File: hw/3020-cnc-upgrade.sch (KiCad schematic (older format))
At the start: 10 parts, among them P1 CONN_01X02, P2 CONN_01X03, P3 CONN_01X08, P4 CONN_01X03, U1 6N136, U2 arduino_pro_micro, U3 MCP41010

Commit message: updated
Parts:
- U2: footprint (none) -> Housings_DIP:DIP-24_W15.24mm
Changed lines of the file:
@@
 F 0 "U2" H 5075 4625 60  0000 C CNN
 F 1 "arduino_pro_micro" H 5275 3225 60  0000 C CNN
-F 2 "" H 5275 3875 60  0001 C CNN
+F 2 "Housings_DIP:DIP-24_W15.24mm" H 5275 3875 60  0001 C CNN
 F 3 "" H 5275 3875 60  0001 C CNN
 	1    5275 3925
@@
 	7500 4375 8100 4375
 $Comp
-L GND #PWR4
+L GND #PWR01
 U 1 1 5A728854
 P 7100 4850
-F 0 "#PWR4" H 7100 4600 50  0001 C CNN
+F 0 "#PWR01" H 7100 4600 50  0001 C CNN
 F 1 "GND" H 7100 4700 50  0000 C CNN
 F 2 "" H 7100 4850 50  0000 C CNN
@@
 	7100 4850 7100 4675
 $Comp
-L +5V #PWR3
+L +5V #PWR02
 U 1 1 5A728882
 P 7100 3675
-F 0 "#PWR3" H 7100 3525 50  0001 C CNN
+F 0 "#PWR02" H 7100 3525 50  0001 C CNN
 F 1 "+5V" H 7100 3815 50  0000 C CNN
 F 2 "" H 7100 3675 50  0000 C CNN
@@
 $EndComp
 $Comp
-L GND #PWR1
+L GND #PWR03
 U 1 1 5A728A6B
 P 3200 4025
-F 0 "#PWR1" H 3200 3775 50  0001 C CNN
+F 0 "#PWR03" H 3200 3775 50  0001 C CNN
 F 1 "GND" H 3200 3875 50  0000 C CNN
 F 2 "" H 3200 4025 50  0000 C CNN
@@
 $EndComp
 $Comp
-L +5V #PWR2
+L +5V #PWR04
 U 1 1 5A72942B
 P 3350 3175
-F 0 "#PWR2" H 3350 3025 50  0001 C CNN
+F 0 "#PWR04" H 3350 3025 50  0001 C CNN
 F 1 "+5V" H 3350 3315 50  0000 C CNN
 F 2 "" H 3350 3175 50  0000 C CNN

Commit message: pcb layout
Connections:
- net ~CS: now reaches U2.13 (10), U3.1 (~CS)
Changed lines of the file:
@@
 Text Label 6050 4075 2    60   ~ 0
 POT
+Text Label 5825 4475 0    60   ~ 0
+~CS
 $EndSCHEMATC

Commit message: minor updates to hw
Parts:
- U1: symbol 6N136 -> 6N136-RESCUE-3020-cnc-upgrade
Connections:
- net +5V: now also P4.3 (P3); no longer P4.1 (P1)
- net GND: now also P4.1 (P1); no longer P4.3 (P3)
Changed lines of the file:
@@
 EESchema Schematic File Version 2
+LIBS:3020-cnc-upgrade-rescue
 LIBS:power
 LIBS:device
@@
 +5V
 $Comp
-L 6N136 U1
+L 6N136-RESCUE-3020-cnc-upgrade U1
 U 1 1 5A728958
 P 2875 3675
@@
 F 3 "" H 7525 2950 50  0000 C CNN
 	1    7525 2950
-	1    0    0    -1
-$EndComp
-Wire Wire Line
+	1    0    0    1
+$EndComp
+Wire Wire Line

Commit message: hardware updates
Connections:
- net +5V: now also P3.8 (P8); no longer P3.1 (P1)
- net GND: now also P3.4 (P4); no longer P3.5 (P5)
- net P3.0/RX: now also P3.2 (P2); no longer P3.7 (P7)
- net P3.1/TX: now also P3.3 (P3); no longer P3.6 (P6)
- net P3.2: now also P3.1 (P1); no longer P3.8 (P8)
- net P3.6: now also P3.7 (P7); no longer P3.2 (P2)
- net P5.4: now also P3.6 (P6); no longer P3.3 (P3)
- net P5.5: now also P3.5 (P5); no longer P3.4 (P4)
- net at P2.1 (P1): now also U3.7 (PB0); no longer U3.5 (PA0)
- net at P2.3 (P3): now also U3.5 (PA0); no longer U3.7 (PB0)
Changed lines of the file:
@@
 F 3 "" H 8300 4275 50  0000 C CNN
 	1    8300 4275
-	1    0    0    -1
+	1    0    0    1
 $EndComp
 $Comp
@@
 F 3 "" H 4600 1725 50  0000 C CNN
 	1    4600 1725
-	1    0    0    -1
+	1    0    0    1
 $EndComp
 Wire Wire Line

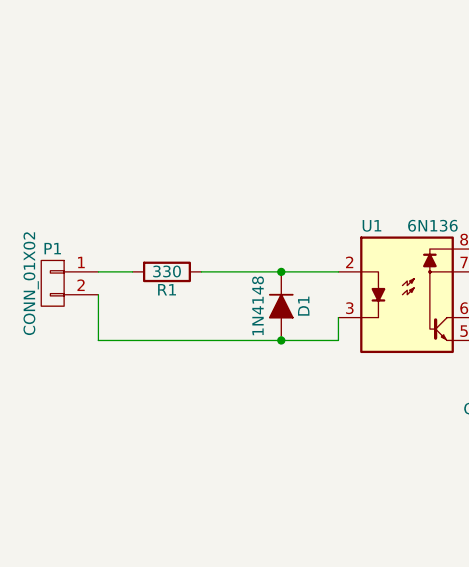
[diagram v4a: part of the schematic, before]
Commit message: swapped pins on pwm input
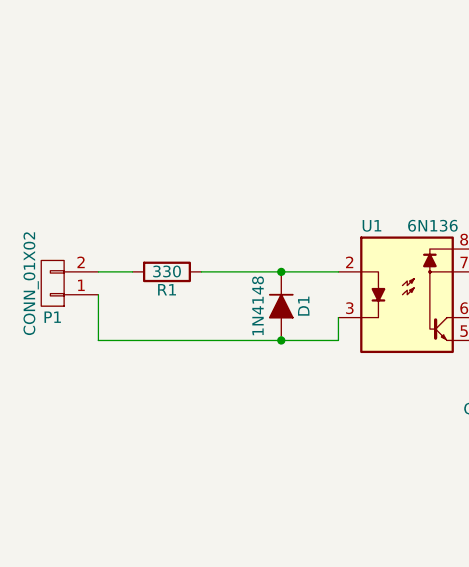
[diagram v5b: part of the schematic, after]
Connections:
- net at D1.2 (A), U1.3: now also P1.1 (P1); no longer P1.2 (P2)
- net at R1.2: now also P1.2 (P2); no longer P1.1 (P1)
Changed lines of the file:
@@
 F 3 "" H 1325 3625 50  0000 C CNN
 	1    1325 3625
-	-1   0    0    -1
+	-1   0    0    1
 $EndComp
 $Comp
